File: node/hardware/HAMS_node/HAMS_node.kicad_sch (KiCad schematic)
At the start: 45 parts, among them J1 Conn_01x02, J2 Conn_02x07_Odd_Even, J3 Conn_01x08, J4 Conn_01x04, J5 Conn_01x04, J6 Conn_01x04, J7 Conn_01x04, Q1 DMP3099L, SW1 TL3305BF100QG, SW2 TL3305BF100QG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

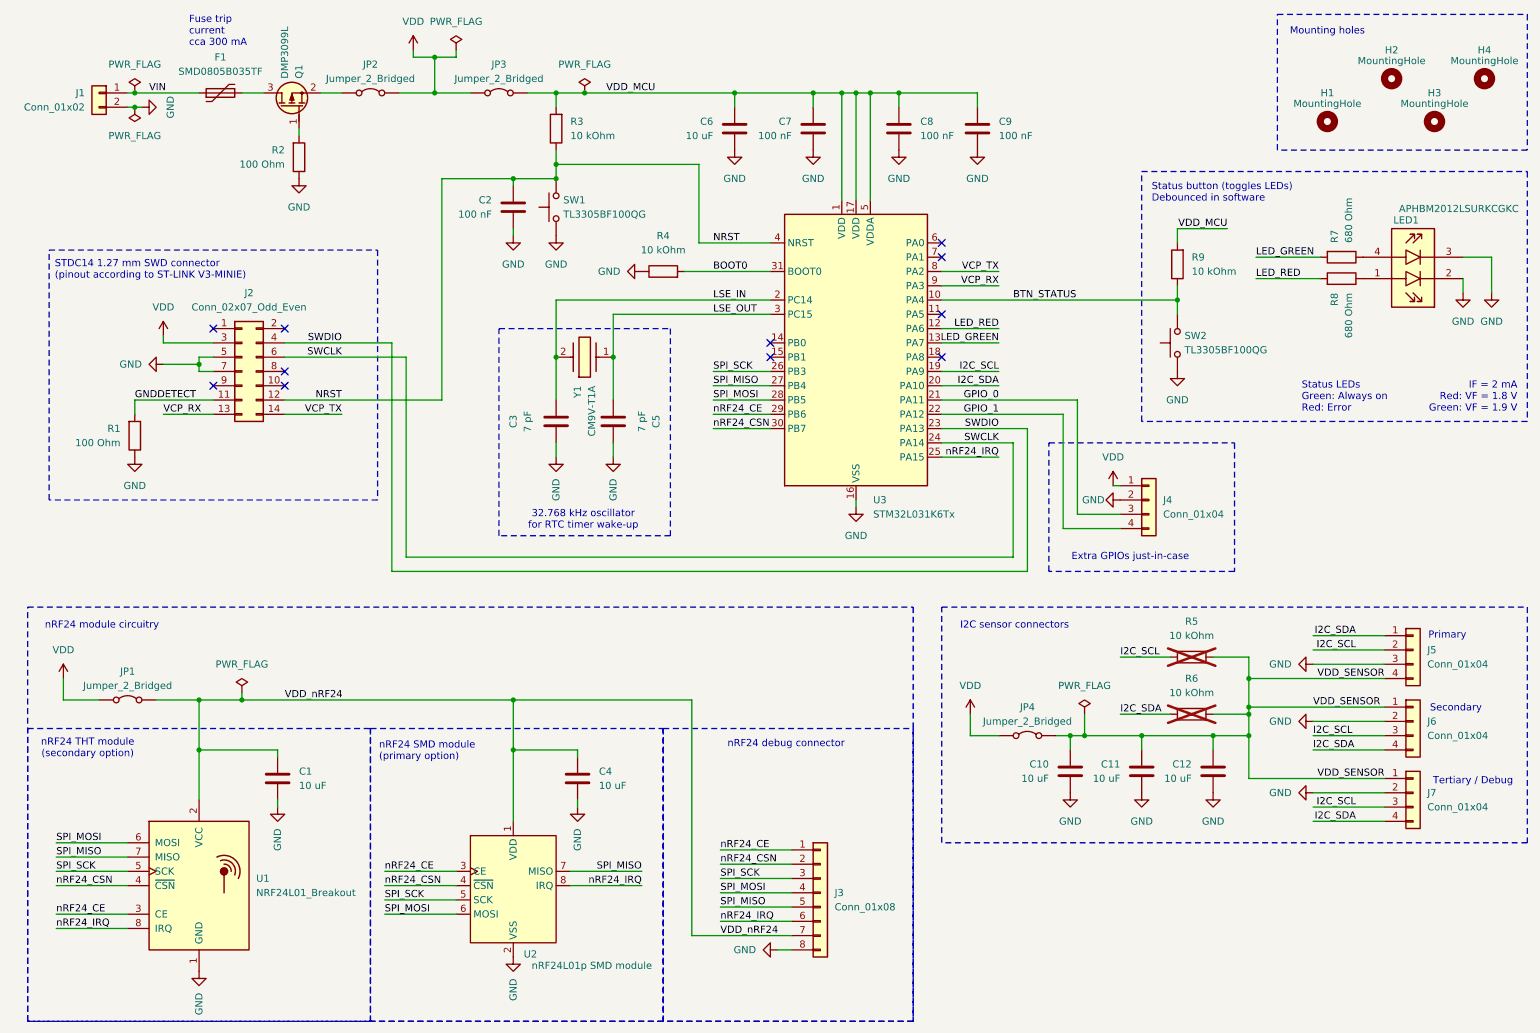
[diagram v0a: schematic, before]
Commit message: Update KiCAD files to version 9
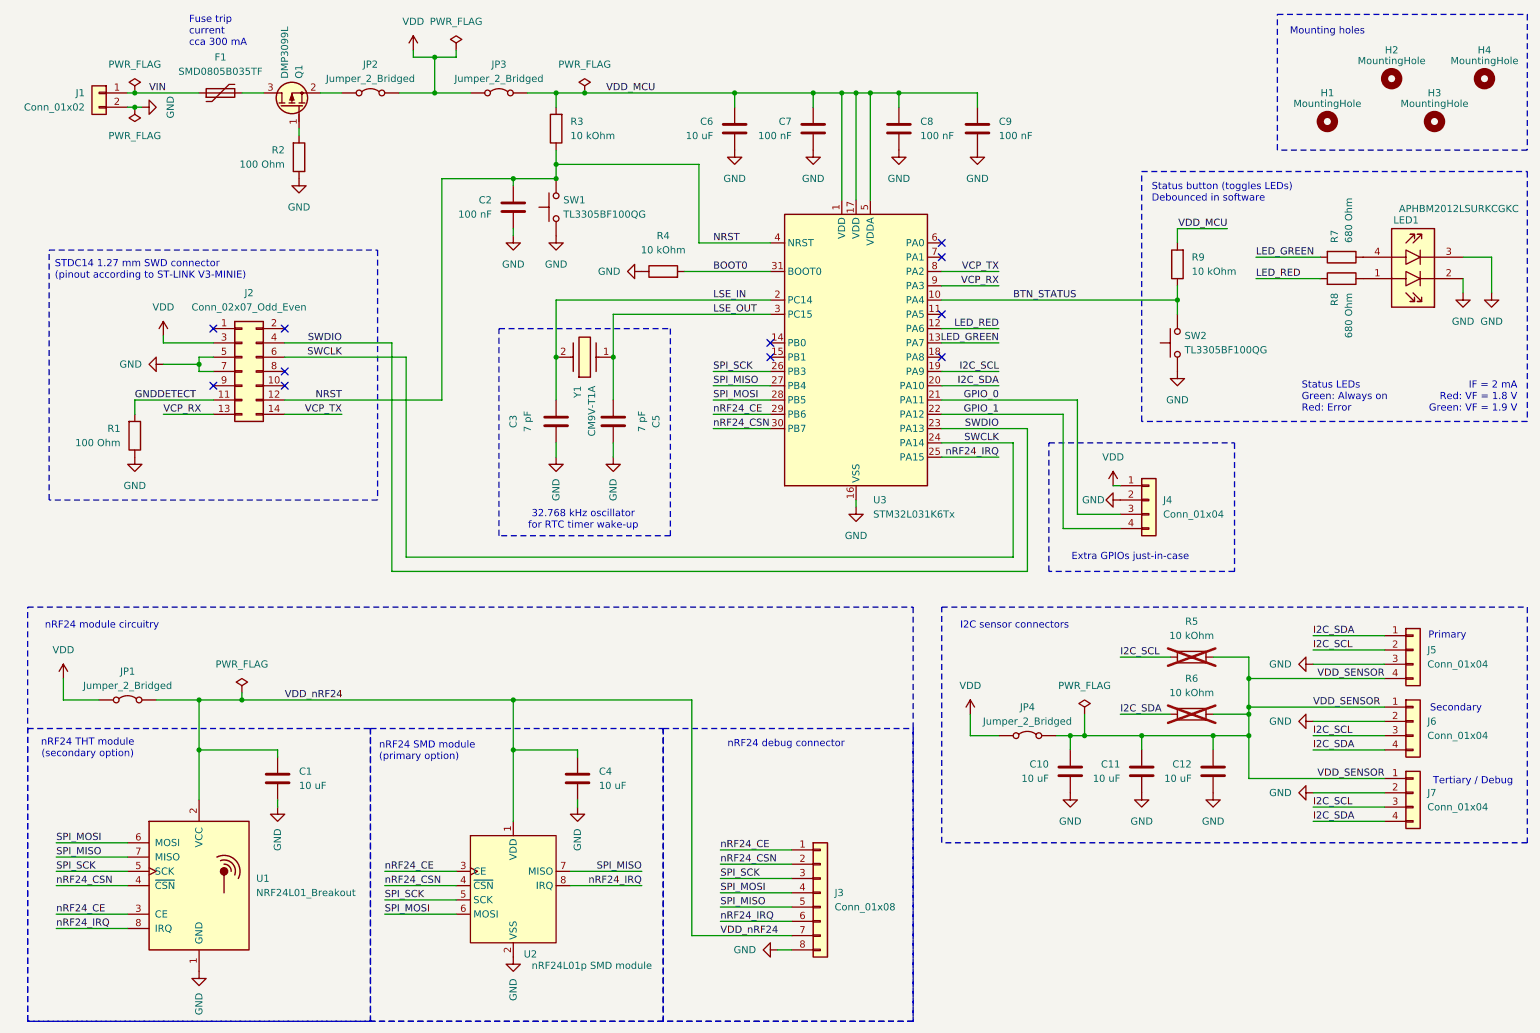
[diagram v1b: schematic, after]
